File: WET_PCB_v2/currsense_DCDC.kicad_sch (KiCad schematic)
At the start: 9 parts, among them J17 Capacitor connector, U1 Opamp_Quad

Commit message: labels
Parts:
- renumbered R60 to JMP22
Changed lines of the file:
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@@
 		(dnp no)
 		(fields_autoplaced yes)
-		(property "Reference" "R60"
+		(property "Reference" "JMP22"
 			(at 102.87 52.07 90)
 			(show_name no)
@@
 			(project "WET_PCB_v2"
 				(path "/13451c35-1666-47d9-9525-8d8125ba1cf3/12f67741-eb23-4832-9e03-479bbedcb04e"
-					(reference "R60")
+					(reference "JMP22")
 					(unit 1)
 				)
 				(path "/13451c35-1666-47d9-9525-8d8125ba1cf3/6ecc05b2-84d4-404f-84e6-8cc19742ad68"
-					(reference "R61")
+					(reference "JMP23")
 					(unit 1)
 				)

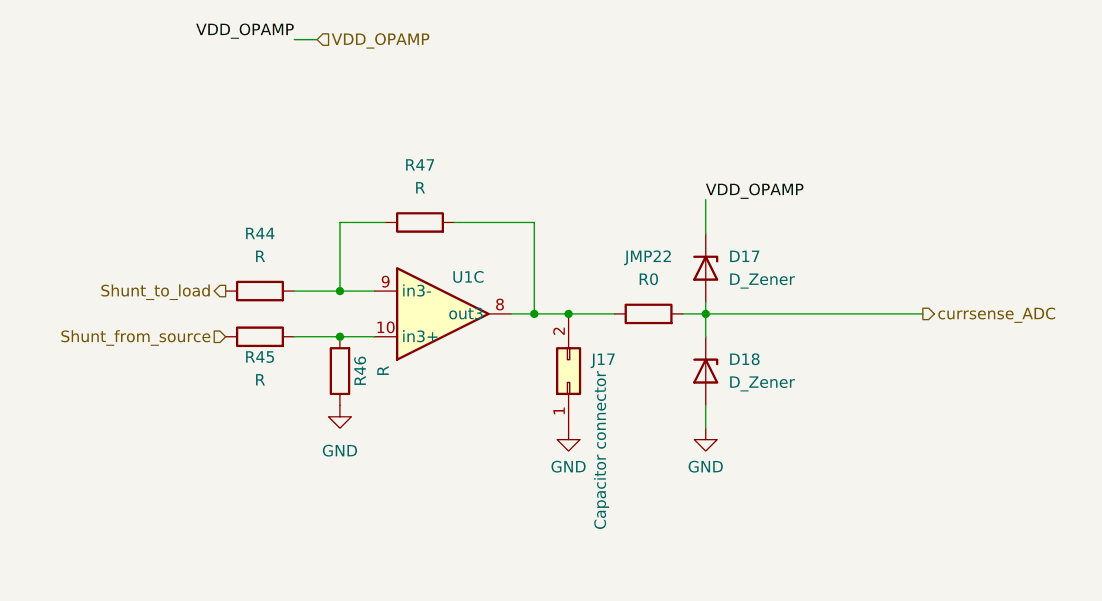
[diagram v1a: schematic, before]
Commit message: added values and notes for assembly
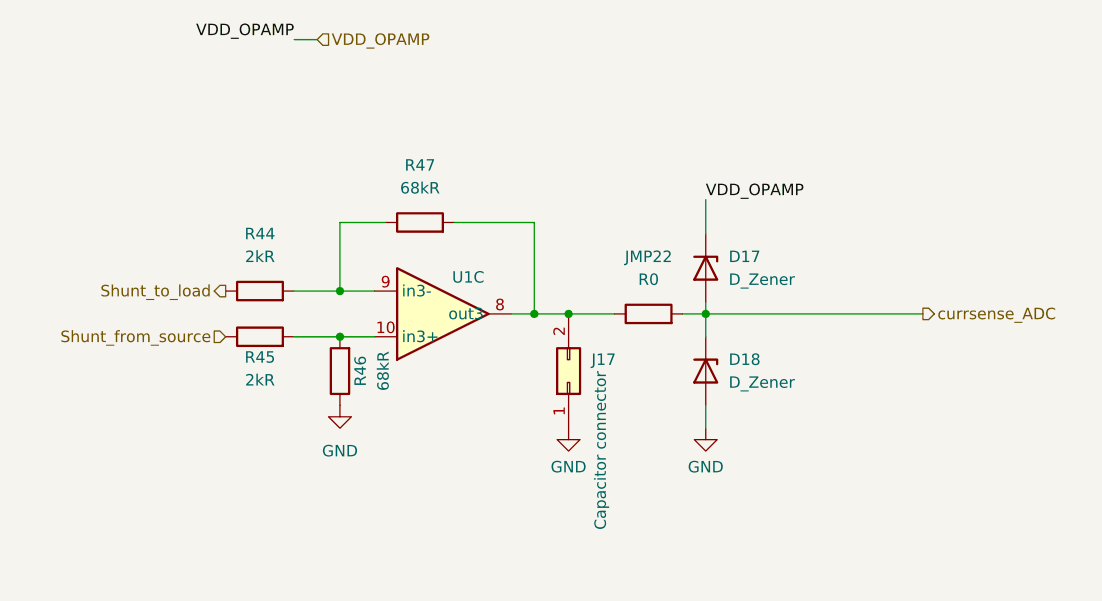
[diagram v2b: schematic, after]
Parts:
- R44, R45: value R -> 2kR
- R46, R47: value R -> 68kR
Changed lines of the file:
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@@
 			)
 		)
-		(property "Value" "R"
+		(property "Value" "2kR"
 			(at 59.69 65.786 90)
 			(show_name no)
@@
 			)
 		)
-		(property "Value" "R"
+		(property "Value" "68kR"
 			(at 77.47 44.45 90)
 			(show_name no)
@@
 			)
 		)
-		(property "Value" "R"
+		(property "Value" "68kR"
 			(at 73.406 64.77 90)
 			(show_name no)
@@
 			)
 		)
-		(property "Value" "R"
+		(property "Value" "2kR"
 			(at 59.69 52.07 90)
 			(show_name no)
